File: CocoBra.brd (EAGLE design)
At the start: 41.9 x 46.9 mm, 20 parts, among them U3 ATTINY84

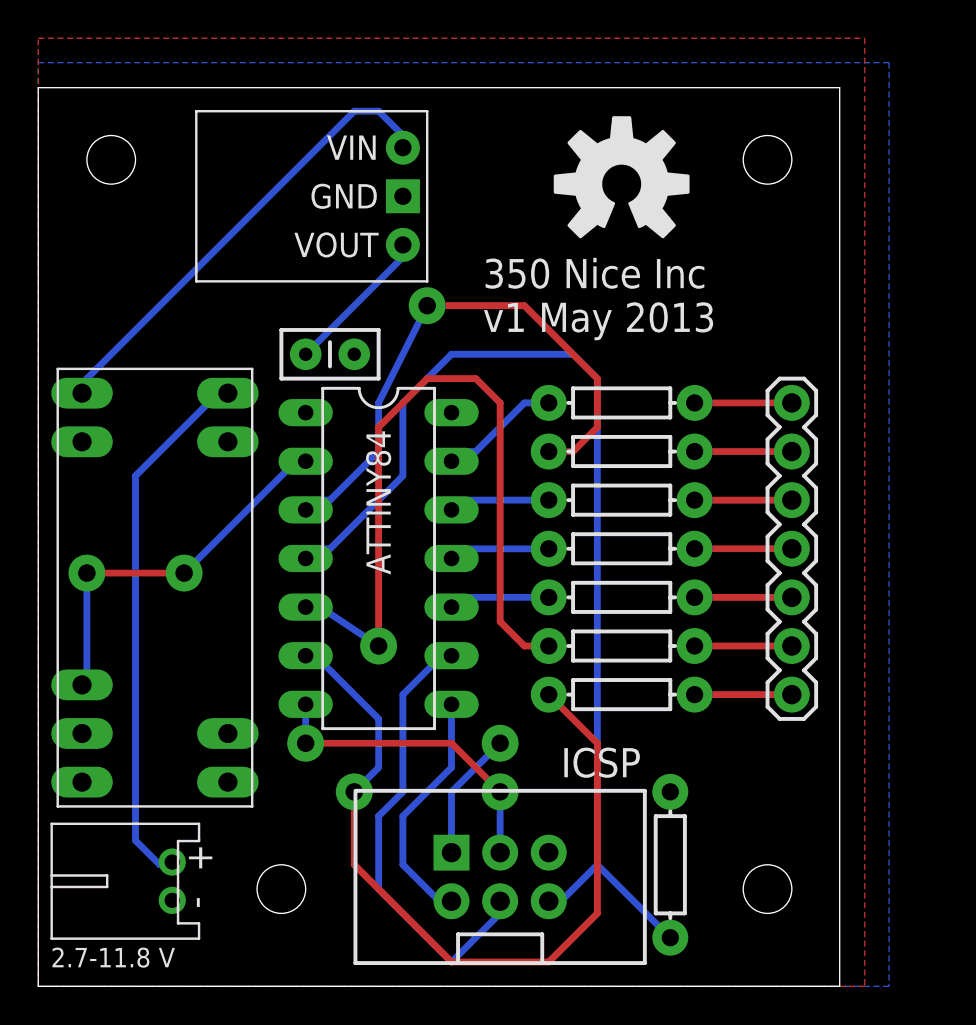
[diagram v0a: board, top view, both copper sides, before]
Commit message: Added tilt switch. EagleUp model taking shape
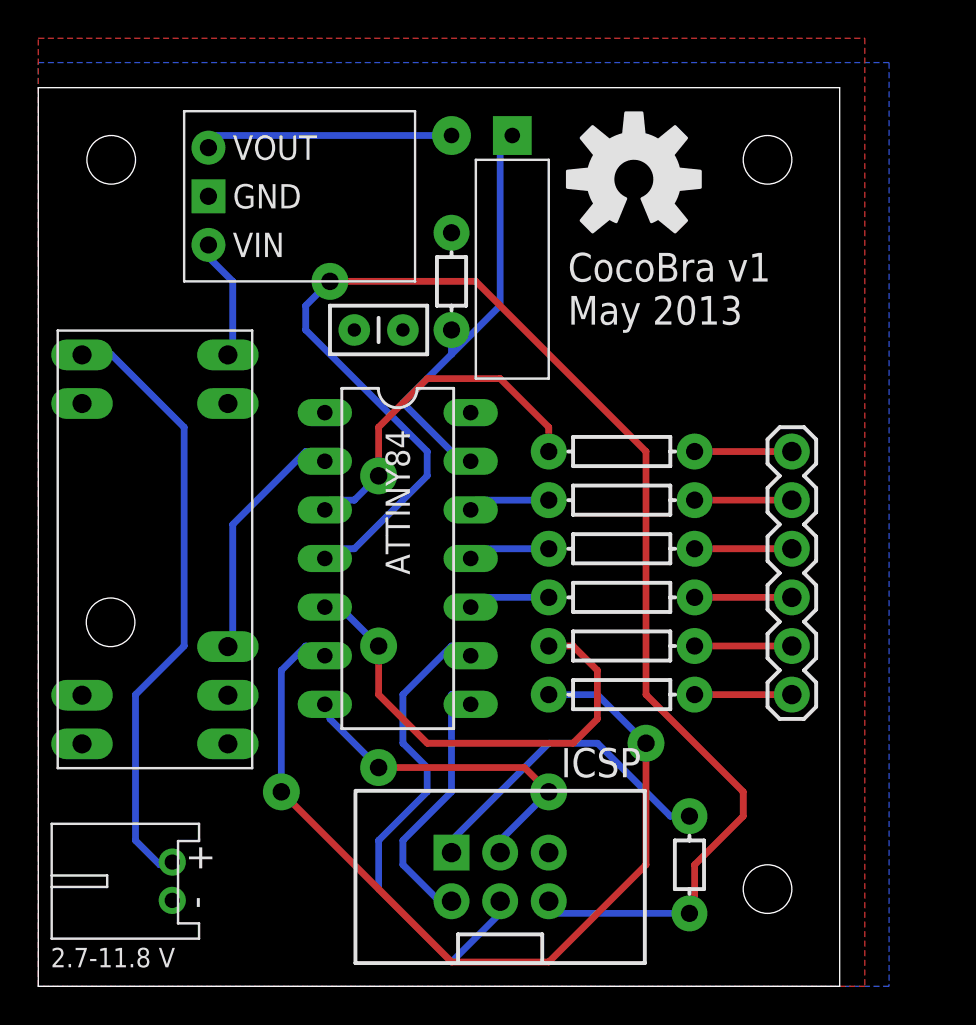
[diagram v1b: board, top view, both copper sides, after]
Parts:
- removed JP1: (no value), SparkFun-Connectors:1X07
- added FRAME1: FRAME-LETTER, SparkFun-Aesthetics:CREATIVE_COMMONS
- added JP2: (no value), SparkFun-Connectors:1X06
- added U$3: SWITCH-SPSTTILT, Dek:SWITCH-SPST-TILT
- R1: device Dek:AXIAL-0.3 -> Dek:AXIAL-0.2
- R8: value 750 -> 10K; device Dek:AXIAL-0.3 -> Dek:AXIAL-0.2
- U$2: value POWER_SUPPLY -> POWER_SUPPLYPOLOLU_S7V7F5; device Dek:POWER_SUPPLY -> Dek:POLOLU_POWER_SUPPLY_S7V7F5
- moved STANDOFF3 16.5 mm to (3.78, 19.0)
- moved U$2 15.5 mm to (7.62, 45.7), turned to 270 degrees
- moved R8 10.9 mm to (21.6, 36.8), turned to 90 degrees
- moved C1 2.84 mm to (16.5, 34.3)
- moved U$4 2.00 mm to (1.02, 11.4)
- moved R1 1.00 mm to (34.0, 6.35)
- moved U3 1.00 mm to (18.8, 22.4)
- moved U$1 0.68 mm to (31.1, 42.2)
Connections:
- removed net JP1: JP1.1, R8.P$2
- net GND: now also R8.P$2
- net JP2: now also JP2.1; no longer JP1.2
- net JP3: now also JP2.2; no longer JP1.3
- net JP4: now also JP2.3; no longer JP1.4
- net JP5: now also JP2.4; no longer JP1.5
- net JP6: now also JP2.5; no longer JP1.6
- net JP7: now also JP2.6; no longer JP1.7
- net N$7: now also U$3.P1
- net VCC: now also U$3.P2
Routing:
- net RST: track 57.7 -> 76.6 mm, vias 0 -> 1
- net VOUT: track 24.3 -> 6.50 mm
- net N$7: track 6.64 -> 22.7 mm
- net VCC: track 14.6 -> 30.4 mm, vias 1 -> 0
- net N$1: track 38.9 -> 25.3 mm
- net N$2: track 29.7 -> 18.4 mm
- net OFF: track 20.5 -> 13.1 mm, vias 2 -> 0
- net JP1: track 5.08 -> 0.00 mm
- net N$3: track 42.4 -> 46.6 mm, vias 1 -> 2
- net VIN: track 28.0 -> 32.0 mm
- net MOSI: track 16.9 -> 19.1 mm
- net SCK: track 24.4 -> 26.1 mm
- net N$6: track 5.59 -> 4.39 mm
- net N$5: track 5.59 -> 4.39 mm
- net N$4: track 5.59 -> 4.39 mm
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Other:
- board text added: "CocoBra v1 May 2013"
- board text removed: "350 Nice Inc v1 May 2013"

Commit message: Exported static docs
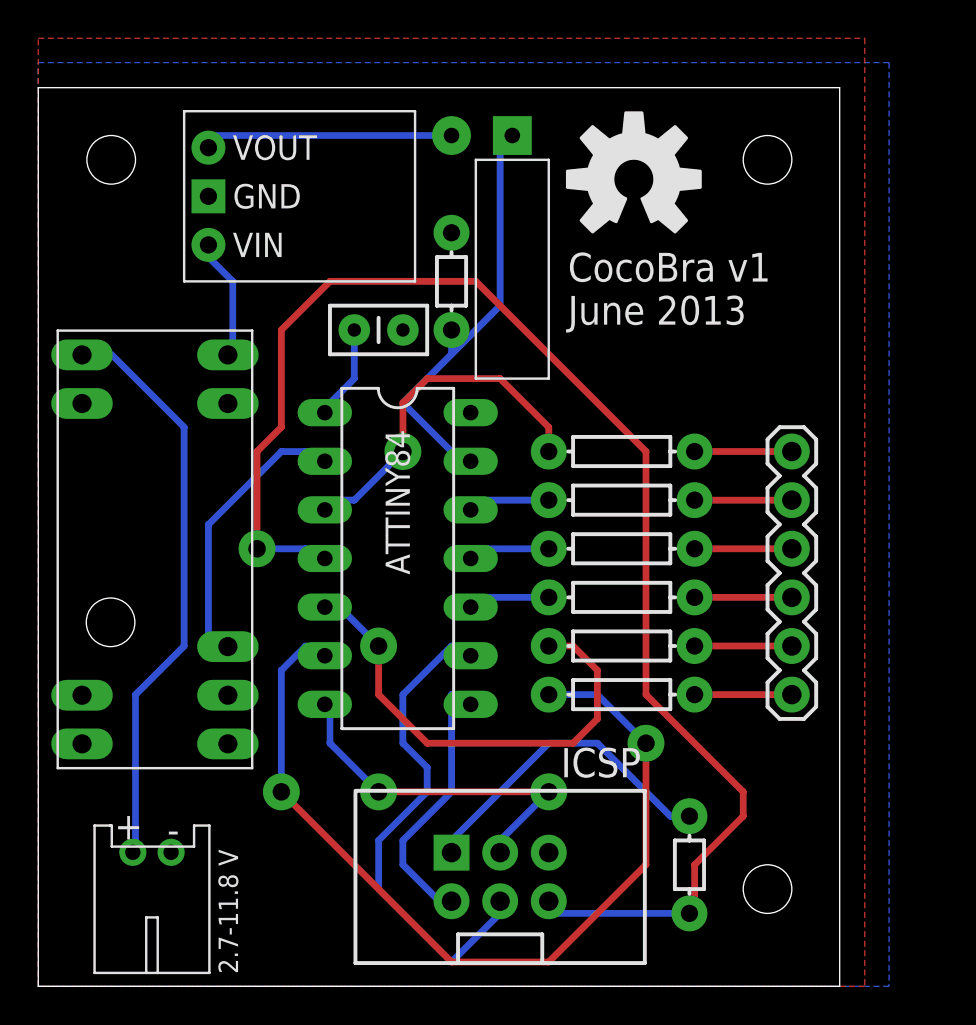
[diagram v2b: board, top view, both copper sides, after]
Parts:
- moved PWR 1.84 mm to (5.94, 7.00), turned to 180 degrees
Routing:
- net VCC: track 30.4 -> 35.3 mm
- net OFF: track 13.1 -> 15.1 mm
- net VIN: track 32.0 -> 30.2 mm
- net RST: track 76.6 -> 75.2 mm
- net MOSI: track 19.1 -> 19.8 mm
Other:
- board text added: "CocoBra v1 June 2013"
- board text removed: "CocoBra v1 May 2013"

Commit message: tagged v1
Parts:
- moved R2 6.35 mm to (36.8, 17.8)
- moved R3 6.35 mm to (36.8, 27.9)
- moved R4 6.35 mm to (36.8, 15.2)
- moved R5 6.35 mm to (36.8, 20.3)
- moved R6 6.35 mm to (36.8, 22.9)
- moved R7 6.35 mm to (36.8, 25.4)
- moved STANDOFF2 5.24 mm to (43.2, 3.81)
- moved JP2 5.08 mm to (44.5, 27.9)
- moved STANDOFF1 5.08 mm to (43.2, 43.2)
- moved U$1 3.81 mm to (34.9, 42.2)
- moved U$3 2.54 mm to (29.2, 43.2)
- moved R8 1.27 mm to (22.9, 36.8)
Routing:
- net RST: track 75.2 -> 40.3 mm
- net N$1: track 25.3 -> 57.7 mm
- net VCC: track 35.3 -> 19.5 mm, vias 0 -> 2
- net VOUT: track 6.50 -> 13.9 mm
- net N$6: track 4.39 -> 10.7 mm
- net N$5: track 4.39 -> 10.7 mm
- net N$4: track 4.39 -> 10.7 mm
- net N$2: track 18.4 -> 24.1 mm
- net MOSI: track 19.8 -> 17.0 mm
- net OFF: track 15.1 -> 13.1 mm
- net JP7: track 5.08 -> 3.81 mm
- net JP6: track 5.08 -> 3.81 mm
- net JP5: track 5.08 -> 3.81 mm
- net JP4: track 5.08 -> 3.81 mm
- net JP3: track 5.08 -> 3.81 mm
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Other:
- board size 41.9 x 46.9 mm -> 46.9 x 46.9 mm
